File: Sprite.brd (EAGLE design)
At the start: 35 x 35 mm, 32 parts, among them P1 SPRITE_PIN, P2 SPRITE_PIN, U1 CC430F5137, U2 HMC5883LSMD, U3 ITG-3200, X1 TCXO_7Z

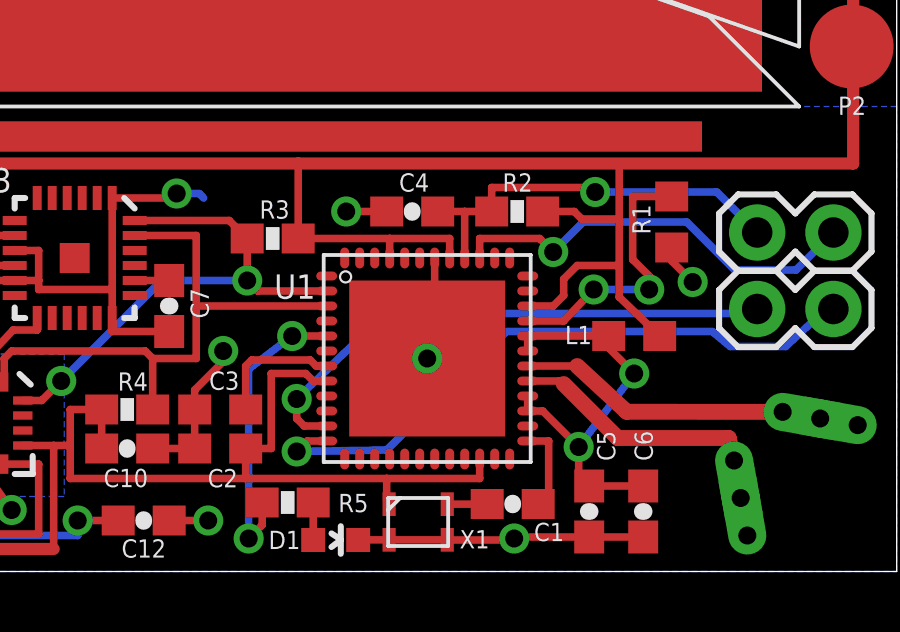
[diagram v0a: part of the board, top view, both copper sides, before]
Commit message: Fixed inconsistency between .brd and .sch
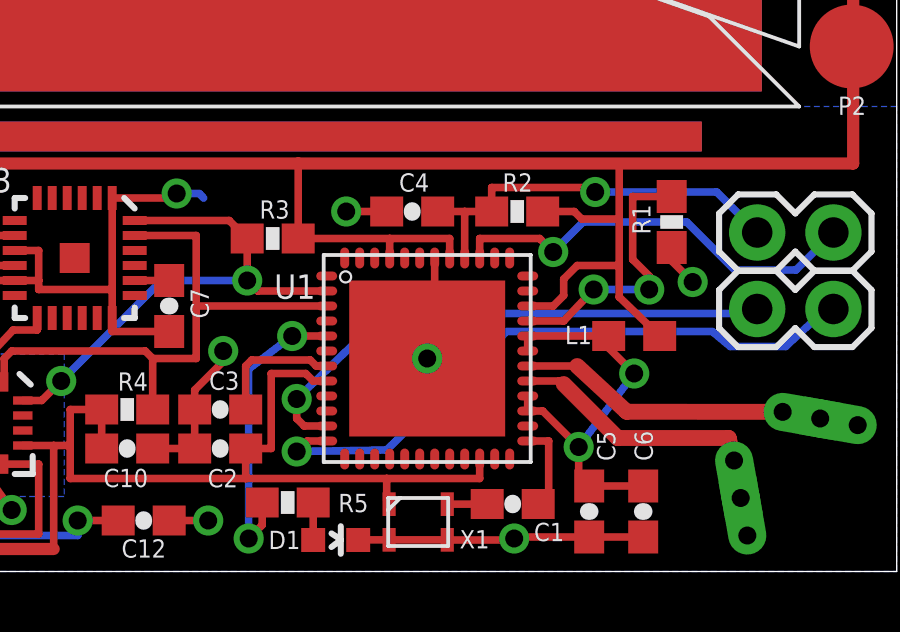
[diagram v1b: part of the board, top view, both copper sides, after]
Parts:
- C2, C3: device rcl:C0603 -> SparkFun:0603-CAP
- R1: device rcl:R0603 -> SparkFun:0603-RES
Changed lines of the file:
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@@
 <?xml version="1.0" encoding="utf-8"?>
 <!DOCTYPE eagle SYSTEM "eagle.dtd">
-<eagle version="6.4">
+<eagle version="6.6.0">
 <drawing>
 <settings>
@@
 <layers>
 <layer number="1" name="Top" color="4" fill="1" visible="yes" active="yes"/>
+<layer number="2" name="Route2" color="1" fill="3" visible="no" active="no"/>
+<layer number="3" name="Route3" color="4" fill="3" visible="no" active="no"/>
+<layer number="14" name="Route14" color="1" fill="6" visible="no" active="no"/>
+<layer number="15" name="Route15" color="4" fill="6" visible="no" active="no"/>
 <layer number="16" name="Bottom" color="1" fill="1" visible="yes" active="yes"/>
 <layer number="17" name="Pads" color="2" fill="1" visible="yes" active="yes"/>
@@
 <attribute name="NAME" x="22.911" y="1.012" size="0.6096" layer="25" font="vector"/>
 </element>
-<element name="R1" library="rcl" package="R0603" value="56K" x="27.5" y="11.65" smashed="yes" rot="R270">
+<element name="R1" library="SparkFun" package="0603-RES" value="56K" x="27.5" y="11.65" smashed="yes" rot="R270">
 <attribute name="NAME" x="26.185" y="12.235" size="0.6096" layer="25" rot="R270"/>
 </element>
-<element name="C2" library="rcl" package="C0603" value="470nF" x="12.45" y="4.1" smashed="yes" rot="R180">
+<element name="C2" library="SparkFun" package="0603-CAP" value="470nF" x="12.45" y="4.1" smashed="yes" rot="R180">
 <attribute name="NAME" x="13.035" y="3.415" size="0.6096" layer="25" rot="R180"/>
 </element>
-<element name="C3" library="rcl" package="C0603" value="470nF" x="12.45" y="5.4" smashed="yes" rot="R180">
+<element name="C3" library="SparkFun" package="0603-CAP" value="470nF" x="12.45" y="5.4" smashed="yes" rot="R180">
 <attribute name="NAME" x="13.085" y="6.665" size="0.6096" layer="25" rot="R180"/>
 </element>

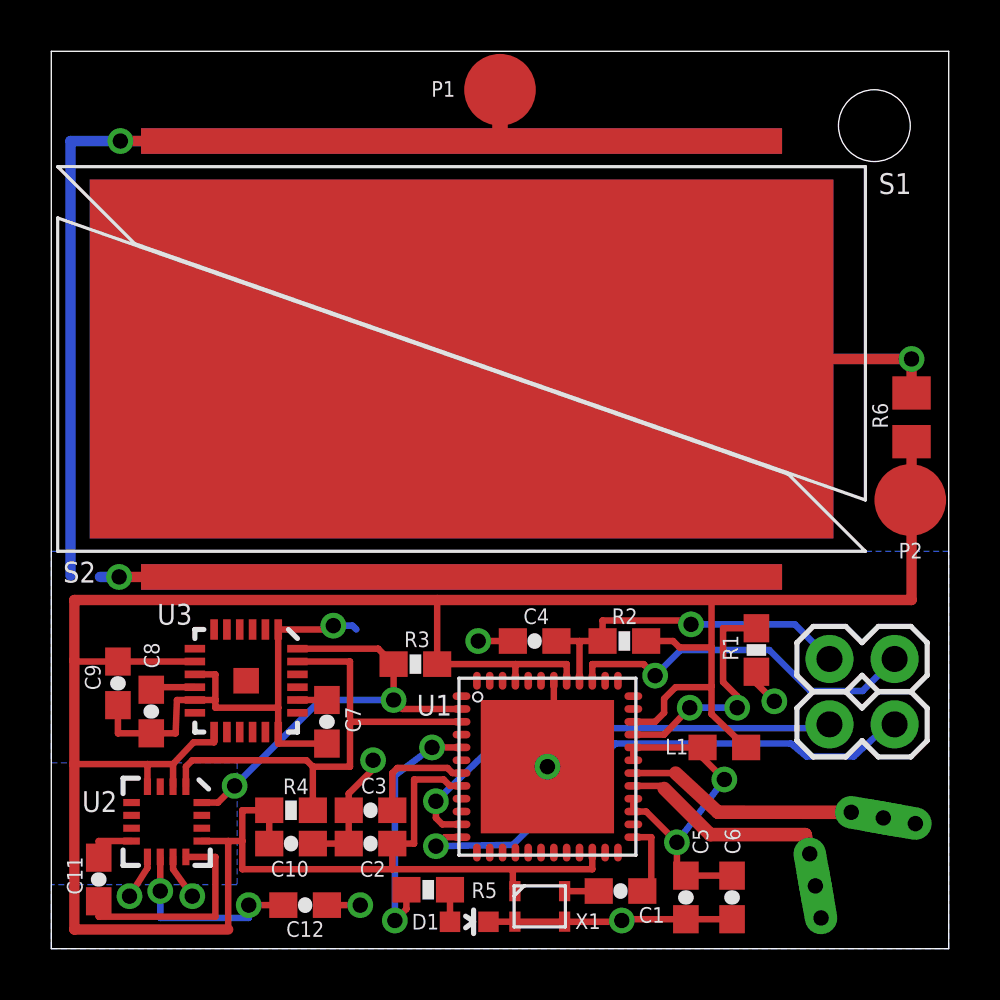
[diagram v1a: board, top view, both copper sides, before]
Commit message: Rolled my own motor driver
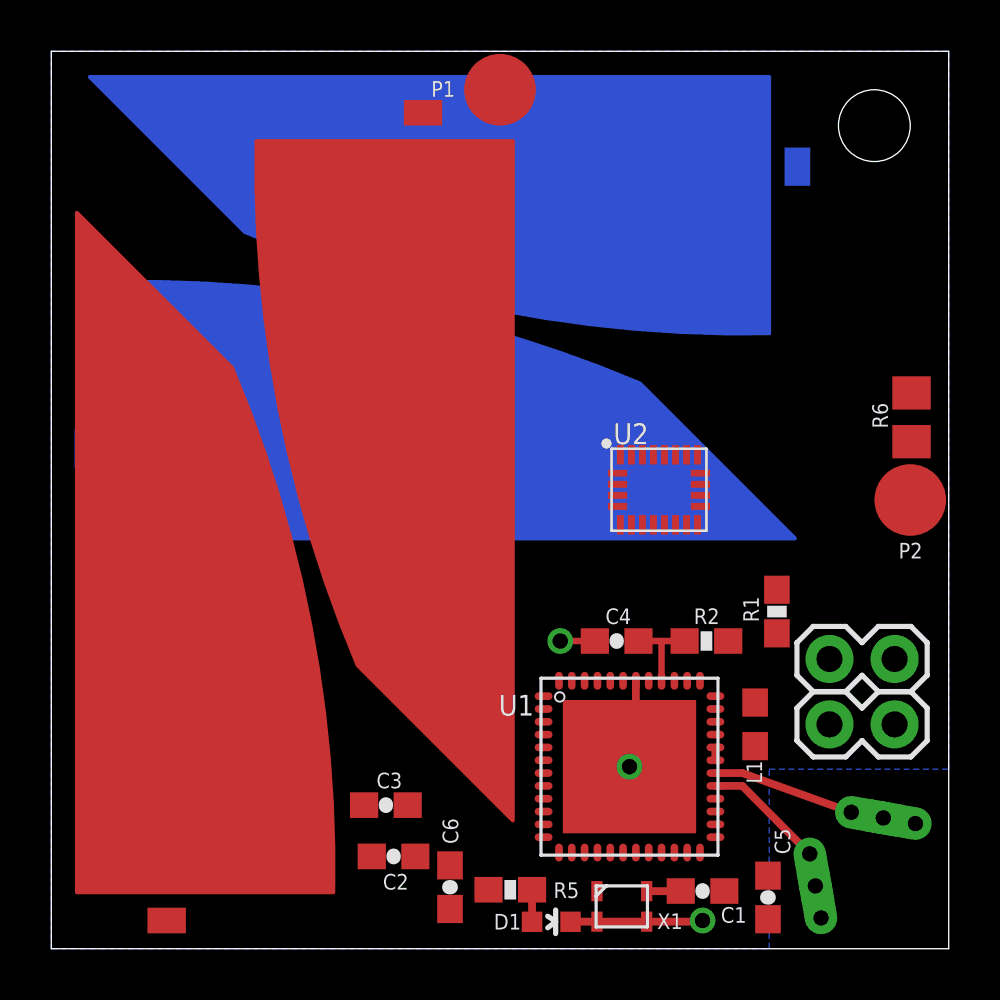
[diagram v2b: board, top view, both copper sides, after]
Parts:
- removed C10, C8: 100nF, SparkFun:0603-CAP
- removed C11: 220nF, SparkFun:0603-CAP
- removed C12: 4.7uF, SparkFun:0603-CAP
- removed C7: 2.2nF, SparkFun:0603-CAP
- removed C9: 10nF, SparkFun:0603-CAP
- removed R3, R4: 4.7K, SparkFun:0603-RES
- removed U3: ITG-3200, SparkFun:QFN-24
- added S3, S4: TRISOLX-WING, TriSolX_QzQube:TRISOLX-T01
- S1, S2: value TASC -> TRISOLX-WING; device TASC:TASC -> TriSolX_QzQube:TRISOLX-T01
- U2: value HMC5883LSMD -> LSM9DS1; device SparkFun:16LPCC -> LSM9DS1:LGA24-8X4
- moved S2 25.6 mm to (1.00, 2.20), flipped to the top, turned to 270 degrees
- moved U2 23.2 mm to (23.7, 17.9), turned to 0 degrees
- moved C6 11.0 mm to (15.6, 2.40)
- moved S1 8.73 mm to (18.0, 31.5), turned to 90 degrees
- moved C1 3.20 mm to (25.4, 2.25)
- moved C4 3.20 mm to (22.1, 12.0)
- moved C5 3.20 mm to (27.9, 2.00)
- moved D1 3.20 mm to (19.5, 1.05)
- moved R2 3.20 mm to (25.6, 12.0)
- moved R5 3.20 mm to (17.9, 2.30)
- moved U1 3.20 mm to (22.6, 7.10)
- moved X1 3.20 mm to (22.2, 1.65)
- moved R1 1.70 mm to (28.3, 13.2)
- moved L1 1.50 mm to (27.4, 8.75), turned to 270 degrees
- moved C2 1.03 mm to (13.3, 3.60)
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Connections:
- removed net N$10: R5.2, U1.5
- removed net N$5: C11.1, U2.8
- removed net N$6: C11.2, U2.12
- removed net N$7: C12.1, U2.10
- removed net N$8: C7.1, U3.20
- removed net N$9: C8.1, U3.10
- removed net RXD: JP3.2, U1.12
- removed net TXD: JP3.1, U1.11
- new net N$2: R5.2, U1.14
- new net UART_RX: JP3.2, U1.6
- new net UART_TX: JP3.1, U1.5
- net GND: now also S1.P$3, S2.P$3, S3.P$3, S4.P$3; no longer C10.2, C12.2, C7.2, C8.2, C9.2, S1.MINUS1, S1.MINUS2, S2.MINUS1, S2.MINUS2, U2.11, U2.9, U3.1, U3.11, U3.18, U3.9
- net SCL: now also U1.9; no longer R4.1, U1.3, U2.1, U3.23
- net SDA: now also U1.10; no longer R3.1, U1.2, U2.16, U3.24
- net VCC: no longer C10.1, C9.1, R3.2, R4.2, U2.13, U2.2, U2.4, U3.13, U3.8
- net VSOLAR: now also S1.P$2, S2.P$2, S3.P$2, S4.P$2; no longer S1.PLUS, S2.PLUS
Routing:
- net VCC: track 123.2 -> 0.00 mm
- net GND: track 109.0 -> 9.99 mm, vias 11 -> 3
- net VSOLAR: track 36.4 -> 0.00 mm, vias 1 -> 0
- net RXD: track 21.3 -> 0.00 mm, vias 1 -> 0
- net SCL: track 19.6 -> 0.00 mm
- net TXD: track 18.3 -> 0.00 mm, vias 1 -> 0
- net SDA: track 17.3 -> 0.00 mm, vias 2 -> 0
- net TEST: track 14.2 -> 0.00 mm, vias 1 -> 0
- net VCCRF: track 14.1 -> 0.50 mm, vias 2 -> 0
- net RST: track 13.6 -> 3.35 mm, vias 1 -> 0
- net N$10: track 10.0 -> 0.00 mm, vias 2 -> 0
- net N$3: track 9.13 -> 0.00 mm, vias 2 -> 0
- net N$6: track 8.63 -> 0.00 mm
- net N$7: track 7.68 -> 0.00 mm, vias 2 -> 0
- net N$4: track 4.32 -> 0.00 mm
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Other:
- board text added: "Sprite v2.6"
- board text removed: "S1"
- board text removed: "S2"
- board text removed: "S3"
- board text removed: "S4"
- board text removed: "Sprite v2.5"

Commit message: Revert "Rolled my own motor driver"
This reverts commit 8d15a71afd97314b3e3036af91b9c243df8797f7.
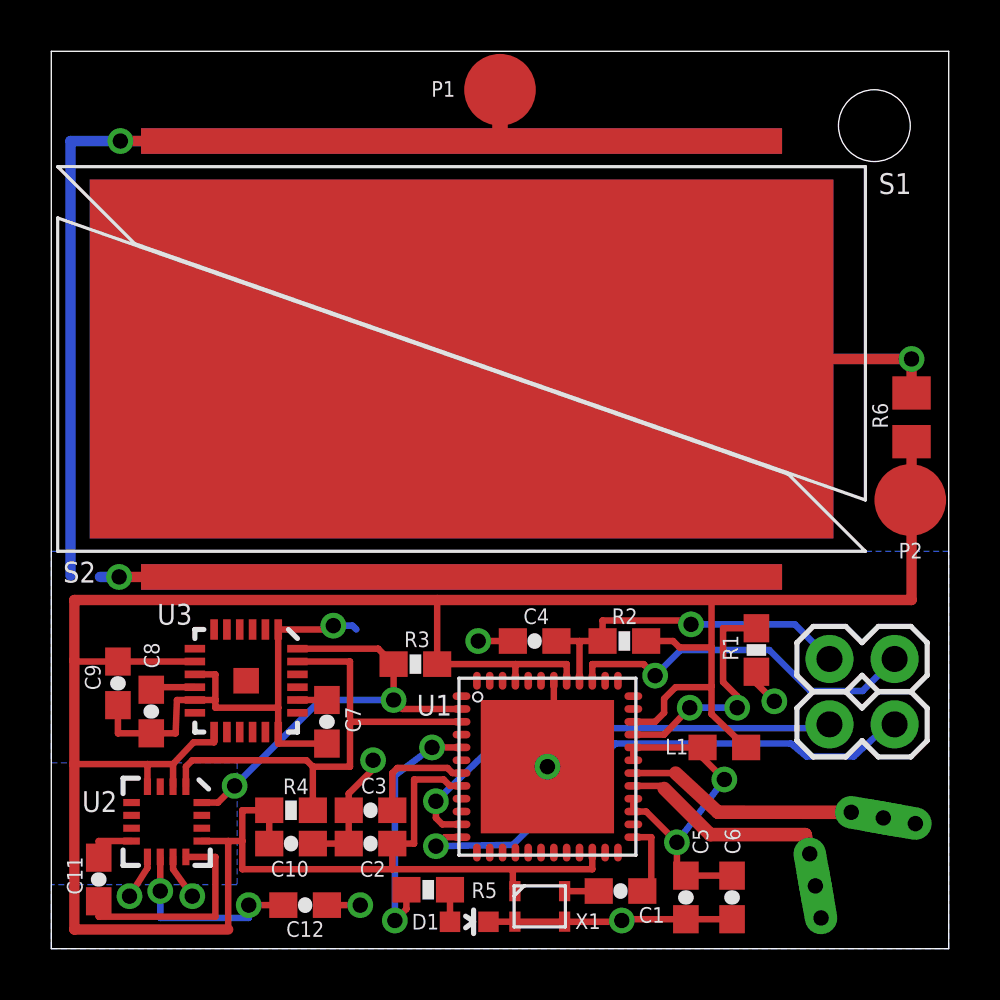
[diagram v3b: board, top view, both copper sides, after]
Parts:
- removed S3, S4: TRISOLX-WING, TriSolX_QzQube:TRISOLX-T01
- added C10, C8: 100nF, SparkFun:0603-CAP
- added C11: 220nF, SparkFun:0603-CAP
- added C12: 4.7uF, SparkFun:0603-CAP
- added C7: 2.2nF, SparkFun:0603-CAP
- added C9: 10nF, SparkFun:0603-CAP
- added R3, R4: 4.7K, SparkFun:0603-RES
- added U3: ITG-3200, SparkFun:QFN-24
- S1, S2: value TRISOLX-WING -> TASC; device TriSolX_QzQube:TRISOLX-T01 -> TASC:TASC
- U2: value LSM9DS1 -> HMC5883LSMD; device LSM9DS1:LGA24-8X4 -> SparkFun:16LPCC
- moved S2 25.6 mm to (16.0, 23.0), flipped to the bottom, turned to 0 degrees
- moved U2 23.2 mm to (4.50, 4.95), turned to 270 degrees
- moved C6 11.0 mm to (26.6, 2.00)
- moved S1 8.73 mm to (16.0, 23.0), turned to 0 degrees
- moved C1 3.20 mm to (22.2, 2.25)
- moved C4 3.20 mm to (18.9, 12.0)
- moved C5 3.20 mm to (24.8, 2.00)
- moved D1 3.20 mm to (16.3, 1.05)
- moved R2 3.20 mm to (22.4, 12.0)
- moved R5 3.20 mm to (14.7, 2.30)
- moved U1 3.20 mm to (19.4, 7.10)
- moved X1 3.20 mm to (19.1, 1.65)
- moved R1 1.70 mm to (27.5, 11.7)
- moved L1 1.50 mm to (26.2, 7.85), turned to 180 degrees
- moved C2 1.03 mm to (12.4, 4.10)
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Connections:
- removed net N$2: R5.2, U1.14
- removed net UART_RX: JP3.2, U1.6
- removed net UART_TX: JP3.1, U1.5
- new net N$10: R5.2, U1.5
- new net N$5: C11.1, U2.8
- new net N$6: C11.2, U2.12
- new net N$7: C12.1, U2.10
- new net N$8: C7.1, U3.20
- new net N$9: C8.1, U3.10
- new net RXD: JP3.2, U1.12
- new net TXD: JP3.1, U1.11
- net GND: now also C10.2, C12.2, C7.2, C8.2, C9.2, S1.MINUS1, S1.MINUS2, S2.MINUS1, S2.MINUS2, U2.11, U2.9, U3.1, U3.11, U3.18, U3.9; no longer S1.P$3, S2.P$3, S3.P$3, S4.P$3
- net SCL: now also R4.1, U1.3, U2.1, U3.23; no longer U1.9
- net SDA: now also R3.1, U1.2, U2.16, U3.24; no longer U1.10
- net VCC: now also C10.1, C9.1, R3.2, R4.2, U2.13, U2.2, U2.4, U3.13, U3.8
- net VSOLAR: now also S1.PLUS, S2.PLUS; no longer S1.P$2, S2.P$2, S3.P$2, S4.P$2
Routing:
- net VCC: track 0.00 -> 123.2 mm
- net GND: track 9.99 -> 109.0 mm, vias 3 -> 11
- net VSOLAR: track 0.00 -> 36.4 mm, vias 0 -> 1
- net RXD: track 0.00 -> 21.3 mm, vias 0 -> 1
- net SCL: track 0.00 -> 19.6 mm
- net TXD: track 0.00 -> 18.3 mm, vias 0 -> 1
- net SDA: track 0.00 -> 17.3 mm, vias 0 -> 2
- net TEST: track 0.00 -> 14.2 mm, vias 0 -> 1
- net VCCRF: track 0.50 -> 14.1 mm, vias 0 -> 2
- net RST: track 3.35 -> 13.6 mm, vias 0 -> 1
- net N$10: track 0.00 -> 10.0 mm, vias 0 -> 2
- net N$3: track 0.00 -> 9.13 mm, vias 0 -> 2
- net N$6: track 0.00 -> 8.63 mm
- net N$7: track 0.00 -> 7.68 mm, vias 0 -> 2
- net N$4: track 0.00 -> 4.32 mm
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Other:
- board text added: "S1"
- board text added: "S2"
- board text added: "S3"
- board text added: "S4"
- board text added: "Sprite v2.5"
- board text removed: "Sprite v2.6"

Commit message: Sprite layout with TrisolX
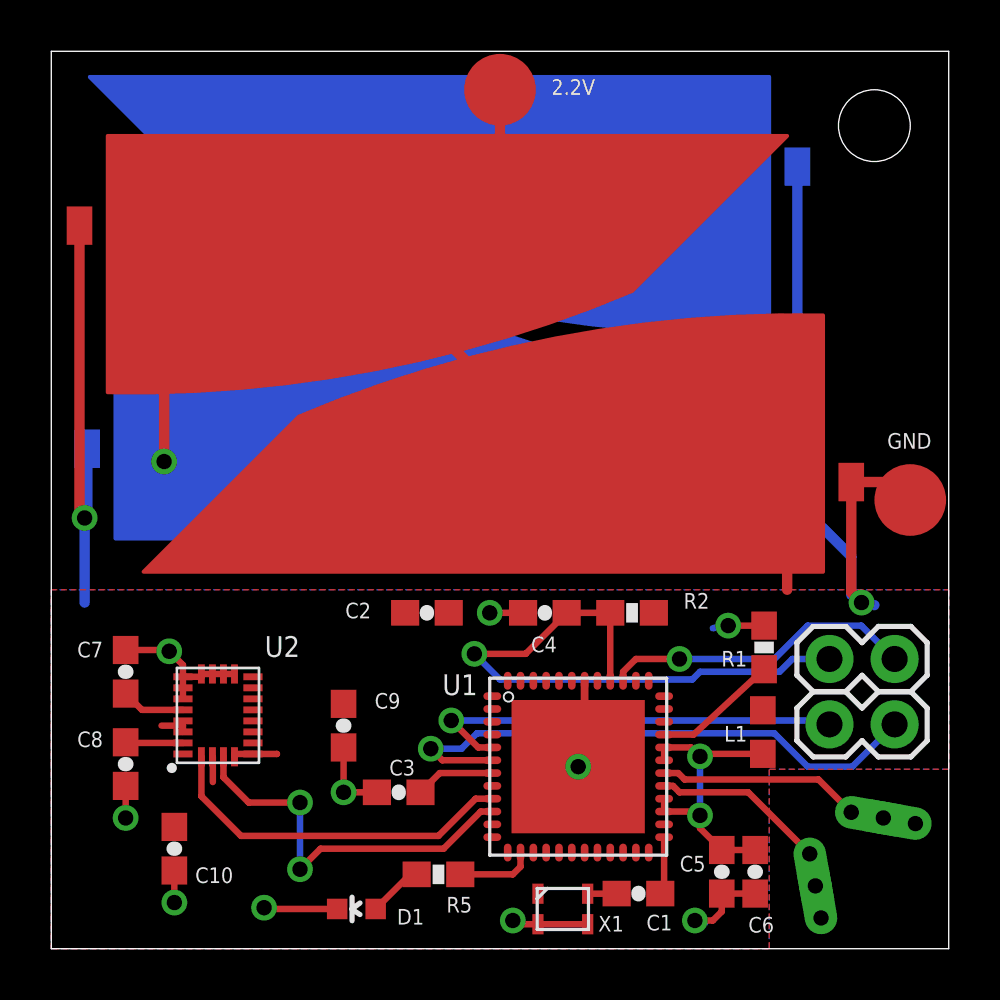
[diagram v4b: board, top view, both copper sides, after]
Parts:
- removed C11: 220nF, SparkFun:0603-CAP
- removed C12: 4.7uF, SparkFun:0603-CAP
- removed R3, R4: 4.7K, SparkFun:0603-RES
- removed R6: 0, rcl:R0805
- removed U3: ITG-3200, SparkFun:QFN-24
- added S3, S4: TRISOLX-WING, TriSolX_QzQube:TRISOLX-T01
- C10: value 100nF -> 10uF
- C7: value 2.2nF -> 10nF
- C8: value 100nF -> 0.1uF
- C9: value 10nF -> 0.1uF
- S1, S2: value TASC -> TRISOLX-WING; device TASC:TASC -> TriSolX_QzQube:TRISOLX-T01
- U2: value HMC5883LSMD -> LSM9DS1; device SparkFun:16LPCC -> LSM9DS1:LGA24-8X4
- moved S1 16.4 mm to (30.1, 14.7)
- moved S2 16.3 mm to (2.20, 31.7), flipped to the top, turned to 180 degrees
- moved C2 9.26 mm to (14.7, 13.1), turned to 0 degrees
- moved C9 8.95 mm to (11.4, 8.70)
- moved C7 8.09 mm to (2.90, 10.8), turned to 90 degrees
- moved U2 4.61 mm to (6.50, 9.10), turned to 90 degrees
- moved C10 4.55 mm to (4.80, 3.90), turned to 270 degrees
- moved D1 4.43 mm to (11.9, 1.55), turned to 90 degrees
- moved C8 2.28 mm to (2.90, 7.20)
- moved C5 1.72 mm to (26.1, 3.00)
- moved L1 1.62 mm to (27.8, 8.45), turned to 270 degrees
- moved C6 1.35 mm to (27.4, 3.00)
- moved C3 1.30 mm to (13.6, 6.10)
- moved U1 1.20 mm to (20.6, 7.10)
- moved C4 1.17 mm to (19.2, 13.1)
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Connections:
- removed net N$10: R5.2, U1.5
- removed net N$7: C12.1, U2.10
- removed net N$8: C7.1, U3.20
- removed net N$9: C8.1, U3.10
- removed net RXD: JP3.2, U1.12
- removed net TXD: JP3.1, U1.11
- removed net VSOLAR: R6.1, S1.PLUS, S2.PLUS
- new net N$2: R5.2, U1.14
- new net UART_RX: JP3.2, U1.6
- new net UART_TX: JP3.1, U1.5
- net GND: now also P2.PIN, S1.P$3, S2.P$3, S3.P$3, S4.P$3, U2.14, U2.15, U2.16, U2.17, U2.18, U2.19, U2.20; no longer C12.2, S1.MINUS1, S1.MINUS2, S2.MINUS1, S2.MINUS2, U2.11, U2.9, U3.1, U3.11, U3.18, U3.9
- net N$5: now also C7.1, U2.21; no longer C11.1, U2.8
- net N$6: now also C8.1, U2.24; no longer C11.2, U2.12
- net SCL: now also U1.9, U2.2; no longer R4.1, U1.3, U2.1, U3.23
- net SDA: now also U1.10, U2.4; no longer R3.1, U1.2, U2.16, U3.24
- net VCC: now also P1.PIN, S1.P$2, S2.P$2, S3.P$2, S4.P$2, U2.1, U2.22, U2.23, U2.3, U2.5, U2.6, U2.7, U2.8; no longer R3.2, R4.2, R6.2, U2.13, U2.2, U2.4, U3.13, U3.8
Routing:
- net VCC: track 123.2 -> 81.5 mm, vias 0 -> 1
- net GND: track 109.0 -> 72.0 mm, vias 11 -> 12
- net VSOLAR: track 36.4 -> 0.00 mm, vias 1 -> 0
- net UART_RX: track 0.00 -> 22.1 mm, vias 0 -> 1
- net RXD: track 21.3 -> 0.00 mm, vias 1 -> 0
- net TXD: track 18.3 -> 0.00 mm, vias 1 -> 0
- net UART_TX: track 0.00 -> 16.8 mm, vias 0 -> 1
- net N$10: track 10.0 -> 0.00 mm, vias 2 -> 0
- net RST: track 13.6 -> 23.2 mm
- net N$7: track 7.68 -> 0.00 mm, vias 2 -> 0
- net N$6: track 8.63 -> 2.25 mm
- net SCL: track 19.6 -> 14.1 mm
- net N$3: track 9.13 -> 4.90 mm, vias 2 -> 0
- net N$2: track 0.00 -> 3.02 mm
- net VCCRF: track 14.1 -> 11.8 mm
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- added copper zone on layer 1, net VCC
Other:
- board text added: "2.2V"
- board text added: "GND"
- board text added: "Sprite v2.6"
- board text removed: "P1"
- board text removed: "P2"
- board text removed: "S1"
- board text removed: "S2"
- board text removed: "S3"
- board text removed: "S4"
- board text removed: "Sprite v2.5"

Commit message: Finished new layout
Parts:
- moved C2 1.01 mm to (14.1, 12.2), turned to 90 degrees
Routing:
- net GND: track 72.0 -> 75.0 mm
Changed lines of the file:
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@@
 <attribute name="NAME" x="27.135" y="11.615" size="0.6096" layer="25" rot="R180"/>
 </element>
-<element name="C2" library="SparkFun" package="0603-CAP" value="470nF" x="14.65" y="13.1" smashed="yes">
-<attribute name="NAME" x="11.465" y="12.885" size="0.6096" layer="25"/>
+<element name="C2" library="SparkFun" package="0603-CAP" value="470nF" x="14.1" y="12.25" smashed="yes" rot="R90">
+<attribute name="NAME" x="14.315" y="9.065" size="0.6096" layer="25" rot="R90"/>
 </element>
 <element name="C3" library="SparkFun" package="0603-CAP" value="470nF" x="13.55" y="6.1" smashed="yes" rot="R180">
@@
 <wire x1="31.2" y1="18.2" x2="32.8" y2="18.2" width="0.4064" layer="1"/>
 <wire x1="32.8" y1="18.2" x2="33.5" y2="17.5" width="0.4064" layer="1"/>
-<wire x1="16.9" y1="13.1" x2="15.5" y2="13.1" width="0" layer="19" extent="1-16"/>
+<wire x1="14.1" y1="13.1" x2="17.1" y2="13.1" width="0.254" layer="1"/>
 </signal>
 <signal name="N$3">
